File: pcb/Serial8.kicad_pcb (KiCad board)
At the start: 2 copper layers, 40 parts, among them J1 USB_B, U1 AM26LV31, U2 CP2102N-A01-GQFN28, U3 AM26LV32

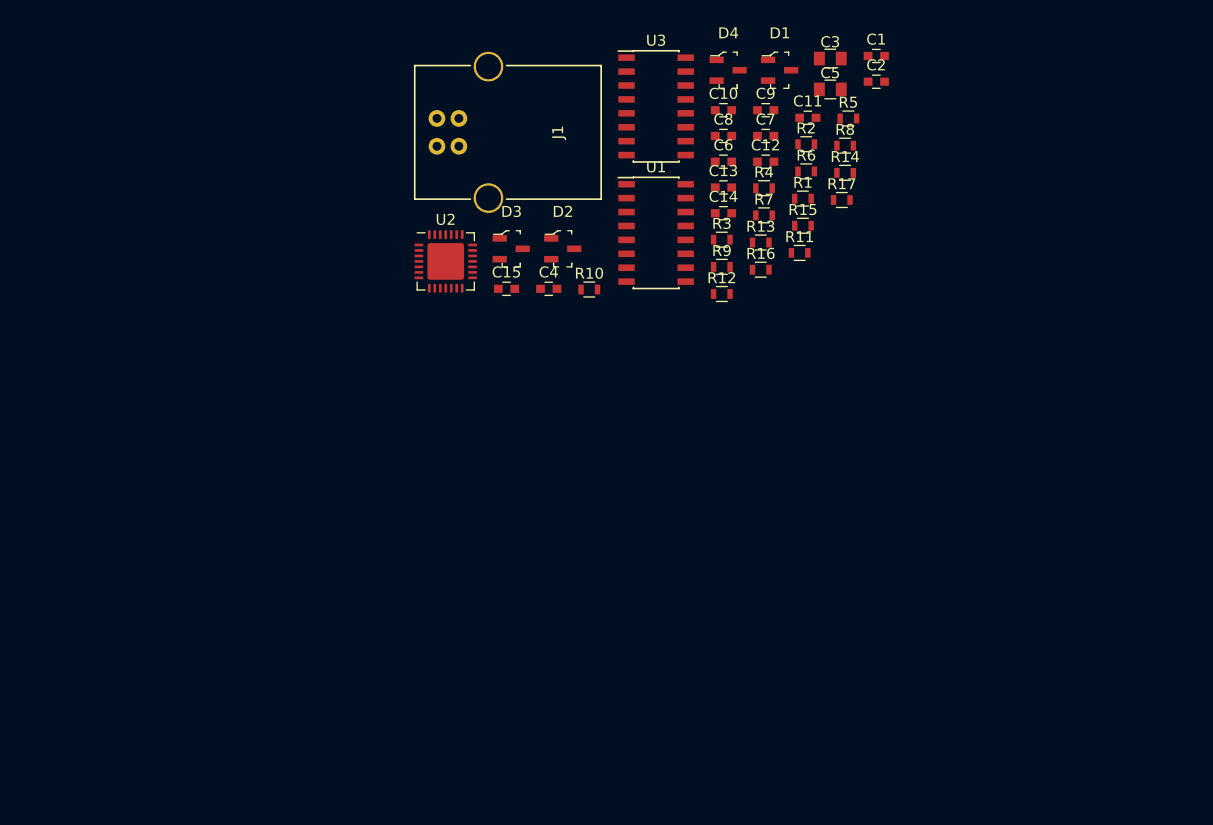
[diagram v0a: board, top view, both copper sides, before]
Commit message: Almost finished layout... but probably need some massive change to make it small enough
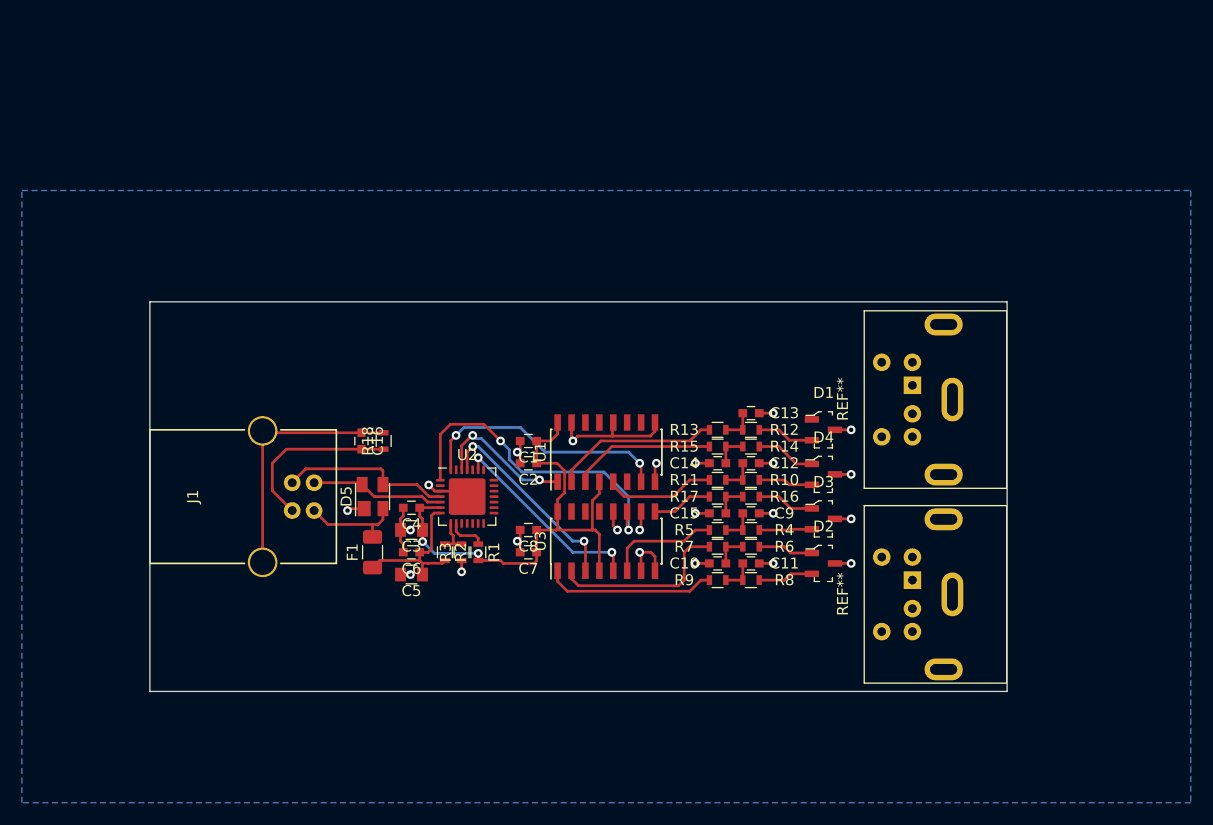
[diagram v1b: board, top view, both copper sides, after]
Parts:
- added C16: 4.7n, Capacitors_SMD:C_0603, F.Cu at (79.2, 121.9)
- added D5: SP0503BAHT, Package_TO_SOT_SMD:SOT-143, F.Cu at (80.3, 127.0)
- added F1: Polyfuse_Small, Fuse:Fuse_1206_3216Metric, F.Cu at (80.3, 132.1)
- added R18: 1M, Resistors_SMD:R_0603, F.Cu at (81.3, 121.9)
- added REF**: Connector_Mini-DIN_Female_6Pin_2rows, Serial8:Connector_Mini-DIN_Female_6Pin_2rows, F.Cu at (129.5, 134.6)
- added REF**: Connector_Mini-DIN_Female_6Pin_2rows, Serial8:Connector_Mini-DIN_Female_6Pin_2rows, F.Cu at (129.5, 116.8)
- moved C5 58.5 mm to (83.8, 134.1), turned to 180 degrees
- moved C3 57.6 mm to (83.8, 130.0), turned to 180 degrees
- moved R2 49.7 mm to (86.9, 132.1), turned to 270 degrees
- moved C1 47.4 mm to (94.5, 121.9), turned to 180 degrees
- moved C2 47.1 mm to (94.5, 124.0), turned to 180 degrees
- moved C6 45.6 mm to (83.8, 132.1), turned to 180 degrees
- moved R1 43.8 mm to (89.9, 132.1), turned to 270 degrees
- moved C7 43.7 mm to (94.5, 132.1), turned to 180 degrees
- moved C10 41.4 mm to (111.8, 133.1), turned to 180 degrees
- moved C11 41.0 mm to (114.8, 133.1)
- moved R8 40.6 mm to (114.8, 134.6)
- moved C8 40.1 mm to (94.5, 130.0), turned to 180 degrees
- moved U3 39.9 mm to (101.6, 131.1), turned to 90 degrees
- moved R5 39.4 mm to (111.8, 130.0)
- moved D4 37.9 mm to (121.4, 125.0)
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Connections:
- D1 pad 1: /TXD+ -> (no net)
- D1 pad 2: /TXD- -> /TXD+
- D3 pad 1: /HSKo -> /GPIn
- D4 pad 1: (no net) -> /TXD-
- D4 pad 2: /GPIn -> /HSKo
- J1 pad 1: (no net) -> Net-(D5-Pad2)
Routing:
- net GND: track 0.00 -> 69.4 mm, vias 0 -> 23
- net +3V3: track 0.00 -> 47.3 mm, vias 0 -> 2
- net /~DCD: track 0.00 -> 29.8 mm, vias 0 -> 2
- net /~DTR: track 0.00 -> 23.5 mm, vias 0 -> 2
- net Net-(C16-Pad1): track 0.00 -> 23.1 mm
- net /RXD: track 0.00 -> 18.8 mm, vias 0 -> 2
- net /~CTS: track 0.00 -> 18.6 mm, vias 0 -> 2
- net /RXD+_EMI: track 0.00 -> 16.5 mm
- net Net-(D5-Pad3): track 0.00 -> 15.8 mm
- net /RXD-_EMI: track 0.00 -> 15.6 mm
- net /TXD+_EMI: track 0.00 -> 15.2 mm
- net +5V: track 0.00 -> 14.0 mm
- net /TXD-_EMI: track 0.00 -> 13.1 mm
- net /TXD: track 0.00 -> 13.1 mm, vias 0 -> 2
- net Net-(D5-Pad4): track 0.00 -> 12.3 mm
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- added copper zone on B.Cu, net GND
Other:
- board outline added: 78.2 x 35.6 mm

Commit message: Rearranged EMI filters and ESD diodes. Board is about 16mm shorter now.
Need to make a MiniDIN8 footprint, and reduce to 1 connector - 2 were in place to cover the ADB version of this PCB (same mounting holes, USB placement, and board size; different DIN count and locations). Mostly same board means mostly same enclosure.
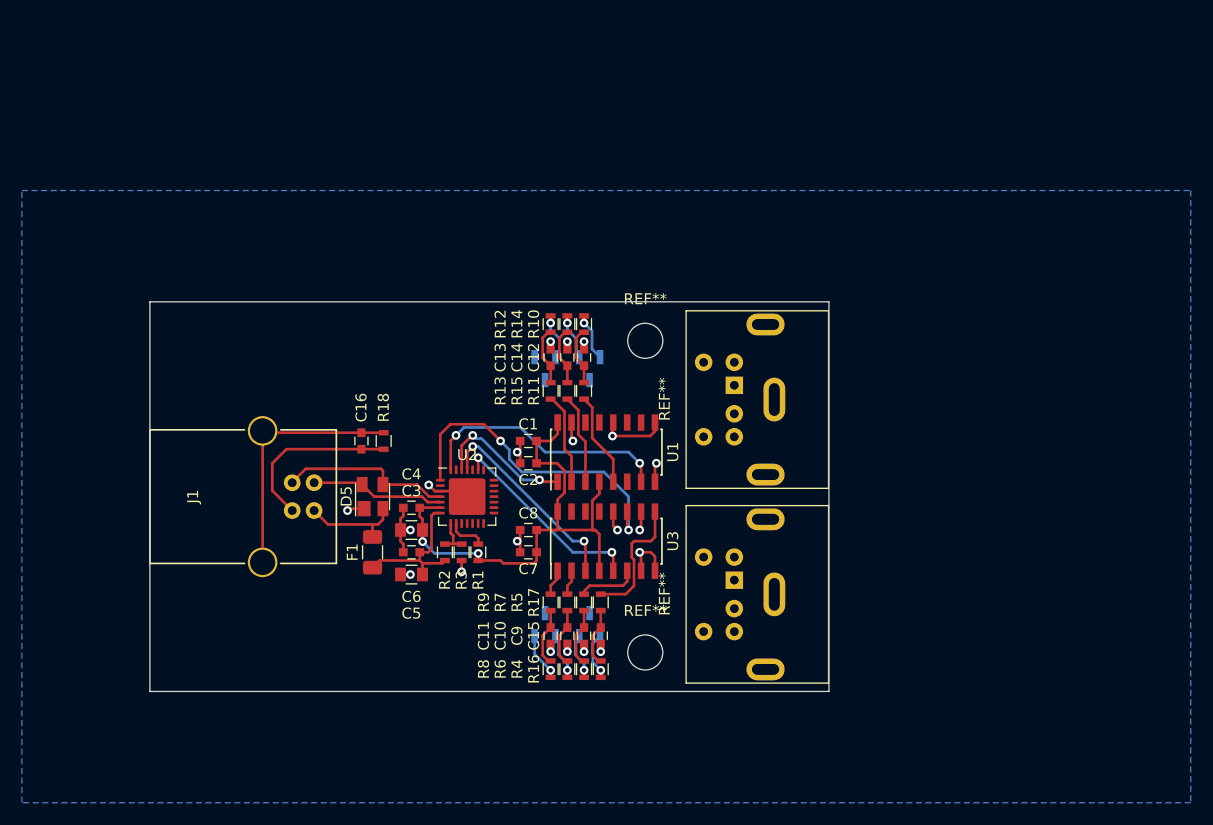
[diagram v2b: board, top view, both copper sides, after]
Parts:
- added REF**: MountingHole_3.2mm_M3_DIN965, MountingHole:MountingHole_3.2mm_M3_DIN965, F.Cu at (105.2, 112.8)
- added REF**: MountingHole_3.2mm_M3_DIN965, MountingHole:MountingHole_3.2mm_M3_DIN965, F.Cu at (105.2, 141.2)
- D1, D2, D3, D4: moved to B.Cu
- moved D1 26.0 mm to (96.0, 115.3), turned to 270 degrees
- moved D2 26.0 mm to (96.0, 138.7), turned to 90 degrees
- moved D4 23.4 mm to (100.1, 115.3), turned to 270 degrees
- moved D3 23.4 mm to (100.1, 138.7), turned to 90 degrees
- moved R16 20.9 mm to (101.1, 142.7), turned to 270 degrees
- moved R10 20.8 mm to (99.6, 111.3), turned to 90 degrees
- moved R12 20.7 mm to (96.5, 111.3), turned to 90 degrees
- moved R14 20.1 mm to (98.0, 111.3), turned to 90 degrees
- moved R6 20.1 mm to (98.0, 142.7), turned to 270 degrees
- moved R8 20.0 mm to (96.5, 142.7), turned to 270 degrees
- moved R4 19.8 mm to (99.6, 142.7), turned to 270 degrees
- moved C11 19.4 mm to (96.5, 139.7), turned to 270 degrees
- moved C13 19.0 mm to (96.5, 114.3), turned to 90 degrees
- moved C9 18.9 mm to (99.6, 139.7), turned to 270 degrees
- moved C12 18.0 mm to (99.6, 114.3), turned to 90 degrees
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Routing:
- net /RXD+_EMI: track 16.5 -> 2.30 mm
- net GND: track 69.4 -> 55.5 mm, vias 23 -> 20
- net /RXD-_EMI: track 15.6 -> 2.40 mm
- net /TXD+_EMI: track 15.2 -> 8.40 mm
- net /GPIn_EMI: track 5.53 -> 12.0 mm
- net /TXD-_EMI: track 13.1 -> 8.22 mm
- net /HSKi_EMI: track 10.3 -> 5.55 mm
- net Net-(C9-Pad1): track 3.07 -> 5.33 mm
- net Net-(C15-Pad1): track 3.07 -> 5.33 mm
- net Net-(C14-Pad1): track 3.07 -> 5.33 mm
- net Net-(C13-Pad1): track 3.07 -> 5.33 mm
- net Net-(C12-Pad1): track 3.07 -> 5.33 mm
- net Net-(C11-Pad1): track 3.07 -> 5.33 mm
- net Net-(C10-Pad1): track 3.07 -> 5.33 mm
- net /HSKo_EMI: track 10.2 -> 8.64 mm
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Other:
- board size 78.2 x 35.6 mm -> 62 x 35.6 mm
